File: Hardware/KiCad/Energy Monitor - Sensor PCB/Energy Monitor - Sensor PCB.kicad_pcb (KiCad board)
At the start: 4 copper layers, 60 x 100 mm, 116 parts, among them IC1 ATM90E36, IC2 ATM90E36, J1 Conn_02x05_Odd_Even, J2 Conn_02x07_Odd_Even, Y1 16.384MHz, Y2 16.384MHz

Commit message: This seems to be getting progressively more complicated. Library cleanup, moved everything to my system library.
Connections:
- J2 pad 2: +3V3 -> +5V

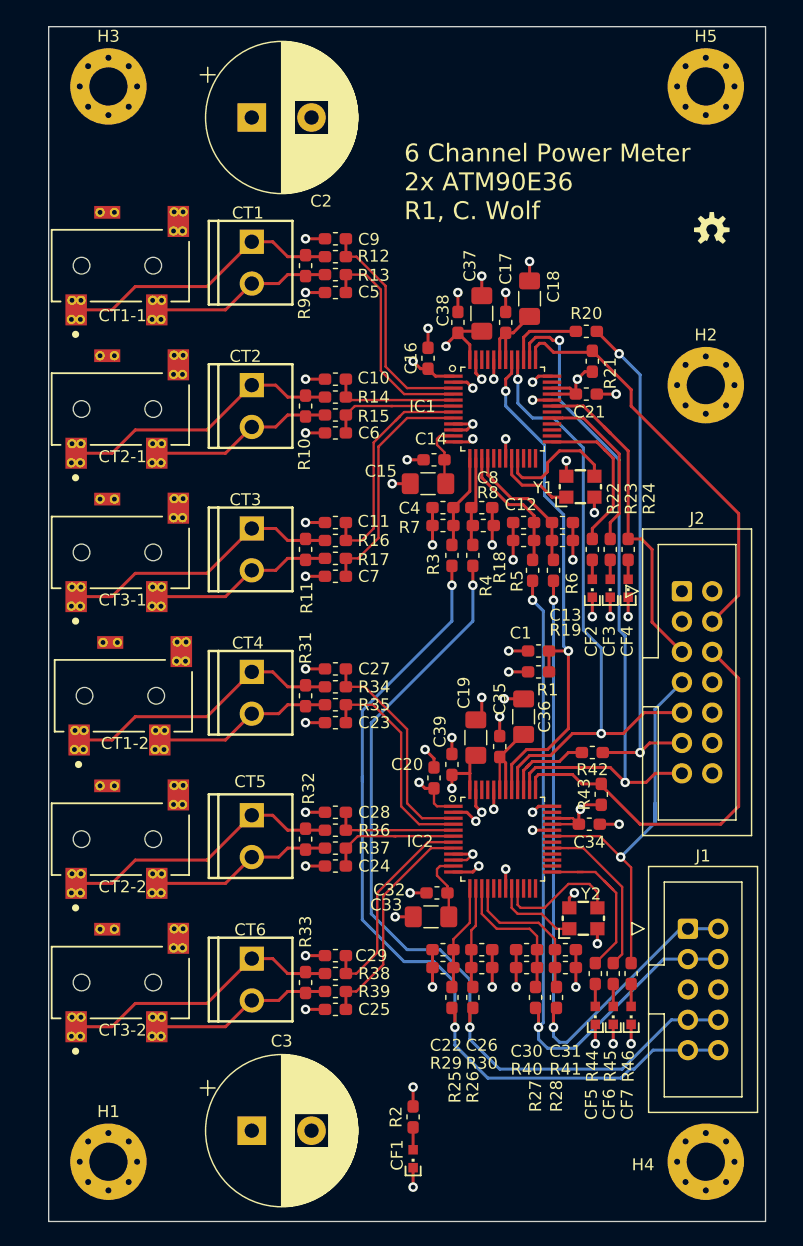
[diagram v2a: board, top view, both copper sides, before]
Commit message: Switch to a better jack.
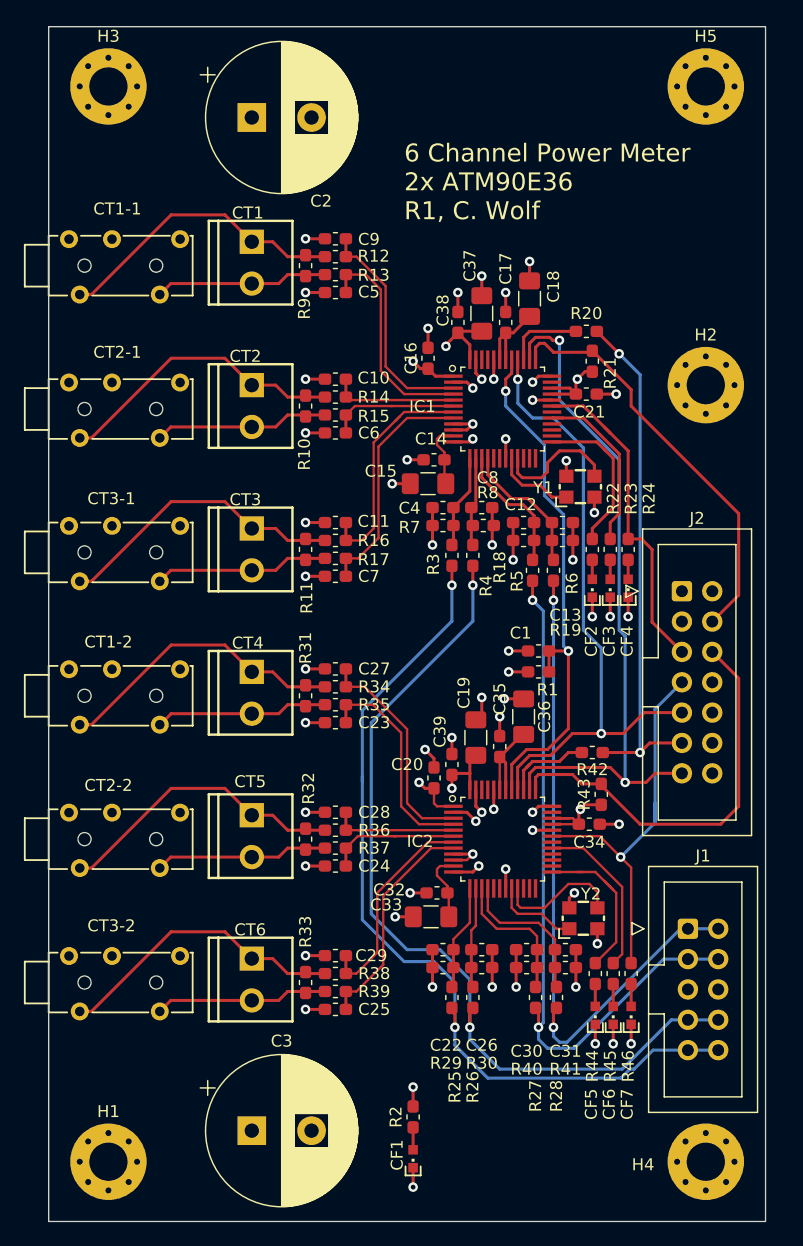
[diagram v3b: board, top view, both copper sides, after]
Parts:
- removed REF**: OSHW-LOGOS, 6_channel_esp32_energy_meter:OSHW-LOGO-S
- CT1-1, CT1-2, CT2-1, CT2-2, CT3-1, CT3-2: footprint 6_channel_esp32_energy_meter:CUI_SJ2-35813B-SMT-TR -> custom:PJ-3270
- moved CT1-2 6.25 mm to (35.0, 91.0), turned to 270 degrees
- moved CT1-1 6.00 mm to (35.0, 55.0), turned to 270 degrees
- moved CT2-1 6.00 mm to (35.0, 67.0), turned to 270 degrees
- moved CT2-2 6.00 mm to (35.0, 103.0), turned to 270 degrees
- moved CT3-1 6.00 mm to (35.0, 79.0), turned to 270 degrees
- moved CT3-2 6.00 mm to (35.0, 115.0), turned to 270 degrees
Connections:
- CT1 pad 1: Net-(CT1-1-Pad1) -> Net-(CT1-1-Pad3)
- CT2 pad 1: Net-(CT2-1-Pad1) -> Net-(CT2-1-Pad3)
- CT3 pad 1: Net-(CT3-1-Pad1) -> Net-(CT3-1-Pad3)
- CT4 pad 1: Net-(CT1-2-Pad1) -> Net-(CT1-2-Pad3)
- CT5 pad 1: Net-(CT2-2-Pad1) -> Net-(CT2-2-Pad3)
- CT6 pad 1: Net-(CT3-2-Pad1) -> Net-(CT3-2-Pad3)
- R10 pad 2: Net-(CT2-1-Pad1) -> Net-(CT2-1-Pad3)
- R11 pad 2: Net-(CT3-1-Pad1) -> Net-(CT3-1-Pad3)
- R12 pad 1: Net-(CT1-1-Pad1) -> Net-(CT1-1-Pad3)
- R14 pad 1: Net-(CT2-1-Pad1) -> Net-(CT2-1-Pad3)
- R16 pad 1: Net-(CT3-1-Pad1) -> Net-(CT3-1-Pad3)
- R31 pad 2: Net-(CT1-2-Pad1) -> Net-(CT1-2-Pad3)
- R32 pad 2: Net-(CT2-2-Pad1) -> Net-(CT2-2-Pad3)
- R33 pad 2: Net-(CT3-2-Pad1) -> Net-(CT3-2-Pad3)
- R34 pad 1: Net-(CT1-2-Pad1) -> Net-(CT1-2-Pad3)
- R36 pad 1: Net-(CT2-2-Pad1) -> Net-(CT2-2-Pad3)
- R38 pad 1: Net-(CT3-2-Pad1) -> Net-(CT3-2-Pad3)
- R9 pad 2: Net-(CT1-1-Pad1) -> Net-(CT1-1-Pad3)
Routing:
- net Net-(CT1-1-Pad3): track 0.00 -> 24.7 mm
- net Net-(CT3-2-Pad3): track 0.00 -> 24.7 mm
- net Net-(CT2-2-Pad3): track 0.00 -> 24.7 mm
- net Net-(CT1-2-Pad3): track 0.00 -> 24.7 mm
- net Net-(CT3-1-Pad3): track 0.00 -> 24.6 mm
- net Net-(CT2-1-Pad3): track 0.00 -> 24.6 mm
- net Net-(CT3-2-Pad1): track 23.7 -> 0.00 mm
- net Net-(CT2-2-Pad1): track 23.7 -> 0.00 mm
- net Net-(CT1-2-Pad1): track 23.7 -> 0.00 mm
- net Net-(CT1-1-Pad1): track 23.7 -> 0.00 mm
- net Net-(CT3-1-Pad1): track 23.6 -> 0.00 mm
- net Net-(CT2-1-Pad1): track 23.6 -> 0.00 mm
- net Net-(CT3-1-Pad2): track 15.4 -> 14.6 mm
- net Net-(CT2-2-Pad2): track 15.3 -> 14.5 mm
- net Net-(CT2-1-Pad2): track 15.4 -> 14.6 mm
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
